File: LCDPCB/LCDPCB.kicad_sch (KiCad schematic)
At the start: 31 parts, among them J1 Sockets, J2 Hot Plug, J3 Programming Header, J4 Conn_01x08_Male, J5 Conn_01x08_Male, SW1 SW_Push, U1 STM32F091RCT6, U2 LD1117S12TR_SOT223

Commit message: minor
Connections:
- net +3.3V: now also C4.1, C5.1, D2.2 (A), U2.2 (VO)
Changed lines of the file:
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@@
   (junction (at 149.86 52.07) (diameter 0) (color 0 0 0 0)
+  )
+  (junction (at 63.5 74.93) (diameter 0) (color 0 0 0 0)
   )
   (junction (at 54.61 101.6) (diameter 0) (color 0 0 0 0)
@@
     (stroke (width 0) (type default) (color 0 0 0 0))
   )
+  (wire (pts (xy 63.5 74.93) (xy 69.85 74.93))
+    (stroke (width 0) (type default) (color 0 0 0 0))
+  )
   (polyline (pts (xy 81.28 55.88) (xy 21.59 55.88))
     (stroke (width 0) (type default) (color 0 0 0 0))
@@
     (stroke (width 0) (type default) (color 0 0 0 0))
   )
-  (wire (pts (xy 59.69 74.93) (xy 69.85 74.93))
+  (wire (pts (xy 59.69 74.93) (xy 63.5 74.93))
     (stroke (width 0) (type default) (color 0 0 0 0))
   )
@@
     (pin "1")
   )
+  (symbol (lib_id "power:+3.3V") (at 63.5 74.93 0) (unit 1)
+    (in_bom yes) (on_board yes) (fields_autoplaced)
+    (property "Reference" "#PWR?" (id 0) (at 63.5 78.74 0)
+      (effects (font (size 1.27 1.27)) hide)
+    )
+    (property "Value" "+3.3V" (id 1) (at 63.5 69.85 0))
+    (property "Footprint" "" (id 2) (at 63.5 74.93 0)
+      (effects (font (size 1.27 1.27)) hide)
+    )
+    (property "Datasheet" "" (id 3) (at 63.5 74.93 0)
+      (effects (font (size 1.27 1.27)) hide)
+    )
+    (pin "1")
+  )
   (symbol (lib_id "power:+3V0") (at 242.57 25.4 0) (unit 1)
     (in_bom yes) (on_board yes) (fields_autoplaced)
@@
       (reference "#PWR0126") (unit 1) (value "+3.3V") (footprint "")
     )
+    (path "/ba82aeb4-706f-462a-8336-75695364b5b1"
+      (reference "#PWR?") (unit 1) (value "+3.3V") (footprint "")
+    )
     (path "/288a3ec0-122f-4360-968a-e07818d05bc7"

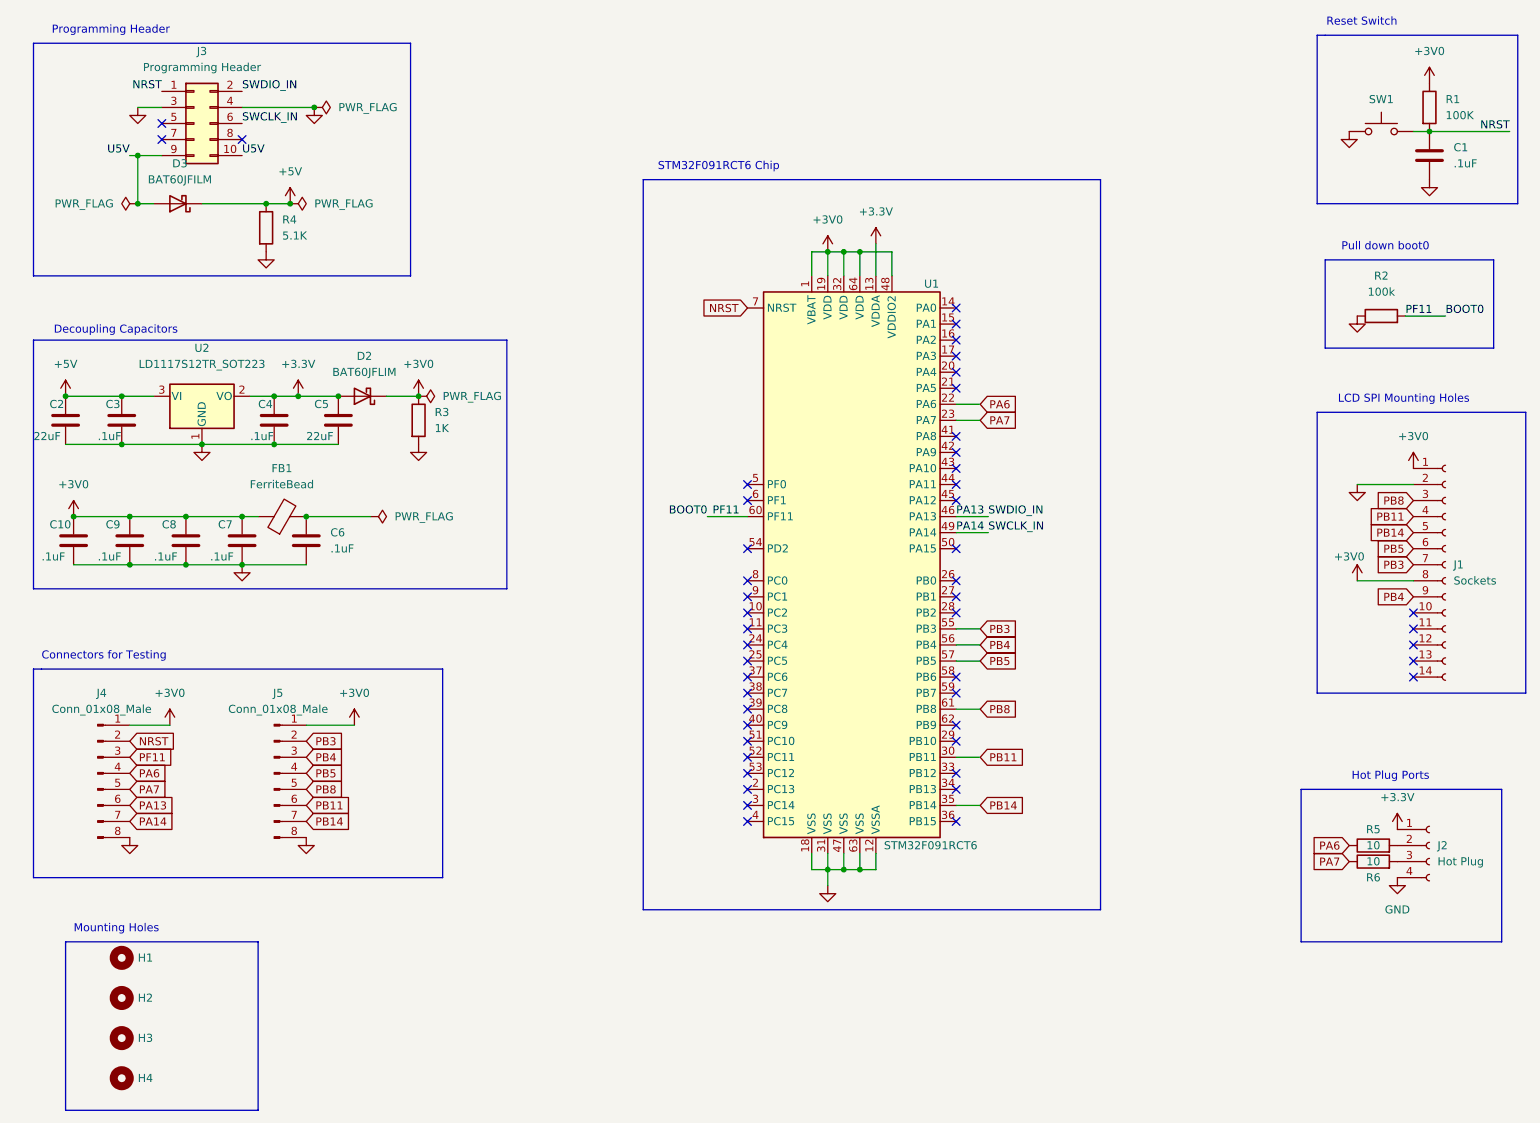
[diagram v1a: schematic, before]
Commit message: added thermal relief, made 5V routes wider
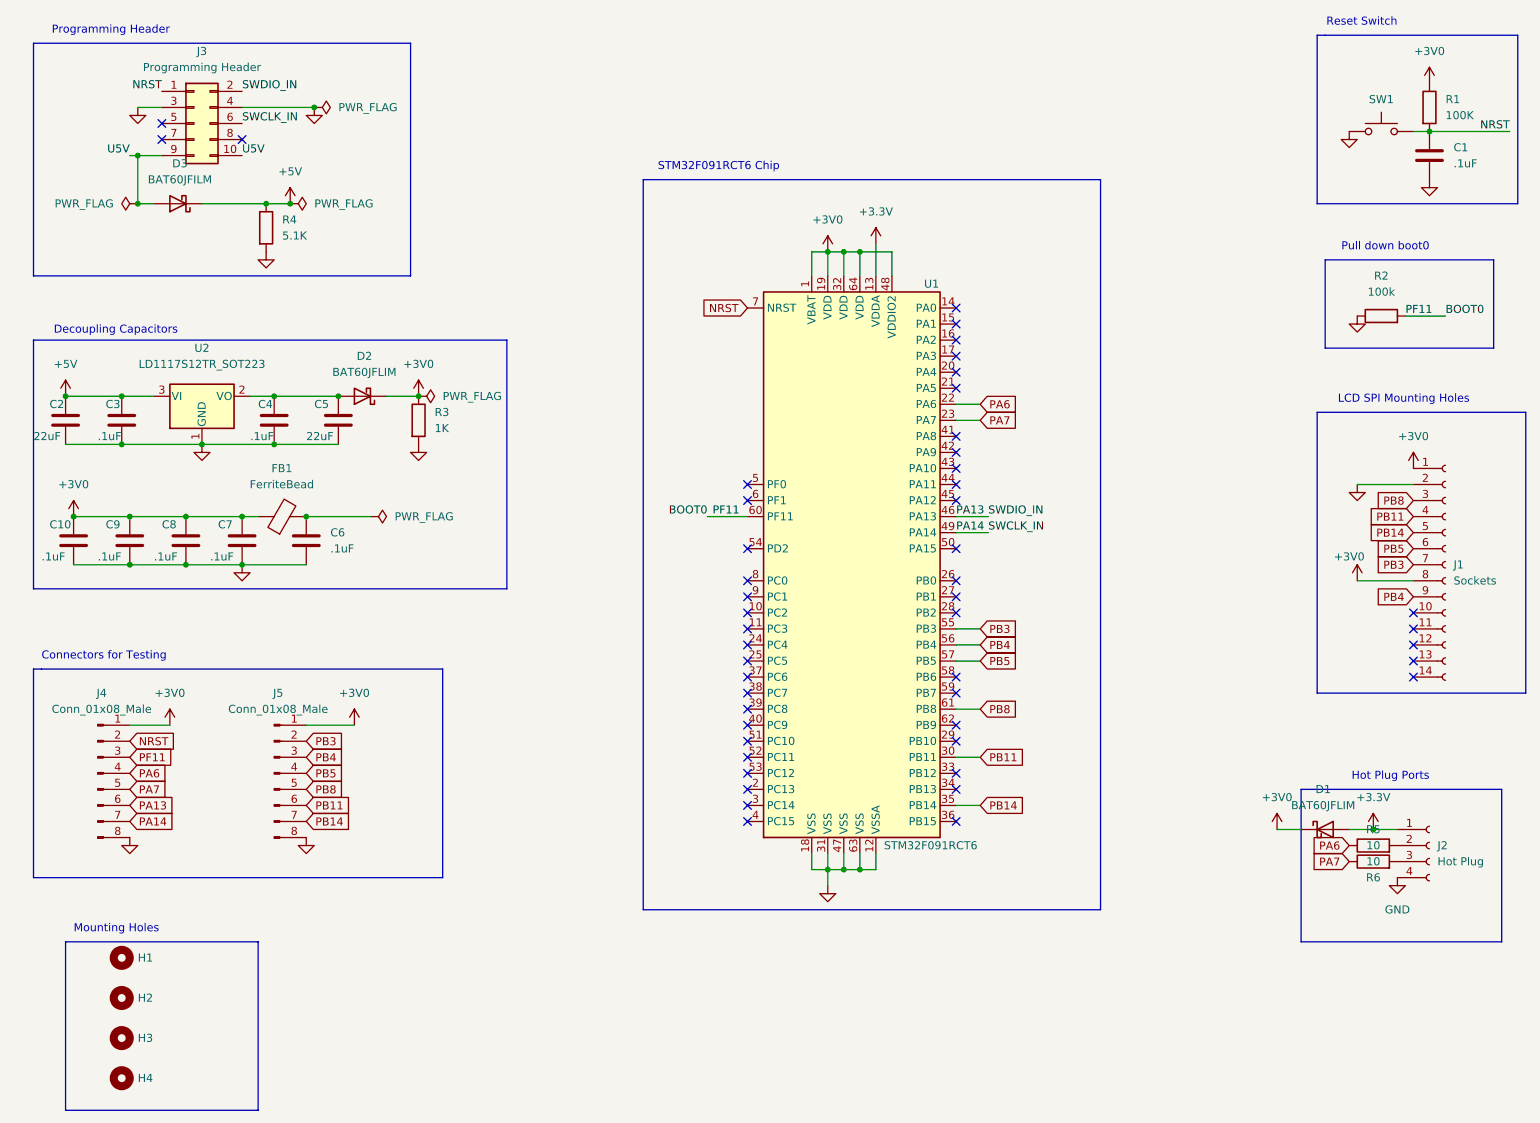
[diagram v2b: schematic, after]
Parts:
- added D1: BAT60JFLIM, lib_file:BAT60JFILM, symbol Diode:BAT60A
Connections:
- net +3.3V: now also D1.2 (A); no longer C4.1, C5.1, D2.2 (A), U2.2 (VO)
- net +3V0: now also D1.1 (K)
- new net: C4.1, C5.1, D2.2 (A), U2.2 (VO)
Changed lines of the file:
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@@
   (junction (at 36.83 101.6) (diameter 0) (color 0 0 0 0)
   )
+  (junction (at 233.68 143.51) (diameter 0) (color 0 0 0 0)
+  )
   (junction (at 62.23 44.45) (diameter 0) (color 0 0 0 0)
   )
@@
   )
   (junction (at 149.86 52.07) (diameter 0) (color 0 0 0 0)
-  )
-  (junction (at 63.5 74.93) (diameter 0) (color 0 0 0 0)
   )
   (junction (at 54.61 101.6) (diameter 0) (color 0 0 0 0)
@@
     (stroke (width 0) (type default) (color 0 0 0 0))
   )
+  (wire (pts (xy 229.87 143.51) (xy 233.68 143.51))
+    (stroke (width 0) (type default) (color 0 0 0 0))
+  )
   (polyline (pts (xy 21.59 118.11) (xy 22.86 118.11))
     (stroke (width 0) (type default) (color 0 0 0 0))
@@
     (stroke (width 0) (type default) (color 0 0 0 0))
   )
-  (wire (pts (xy 63.5 74.93) (xy 69.85 74.93))
+  (wire (pts (xy 59.69 74.93) (xy 69.85 74.93))
     (stroke (width 0) (type default) (color 0 0 0 0))
   )
@@
     (stroke (width 0) (type default) (color 0 0 0 0))
   )
+  (wire (pts (xy 218.44 143.51) (xy 222.25 143.51))
+    (stroke (width 0) (type default) (color 0 0 0 0))
+  )
   (wire (pts (xy 36.83 101.6) (xy 45.72 101.6))
     (stroke (width 0) (type default) (color 0 0 0 0))
@@
     (stroke (width 0) (type default) (color 0 0 0 0))
   )
+  (wire (pts (xy 233.68 143.51) (xy 237.49 143.51))
+    (stroke (width 0) (type default) (color 0 0 0 0))
+  )
   (wire (pts (xy 147.32 52.07) (xy 149.86 52.07))
     (stroke (width 0) (type default) (color 0 0 0 0))
@@
   )
   (wire (pts (xy 77.47 74.93) (xy 82.55 74.93))
-    (stroke (width 0) (type default) (color 0 0 0 0))
-  )
-  (wire (pts (xy 59.69 74.93) (xy 63.5 74.93))
     (stroke (width 0) (type default) (color 0 0 0 0))
   )
@@
     (pin "2")
   )
+  (symbol (lib_id "Diode:BAT60A") (at 226.06 143.51 0) (unit 1)
+    (in_bom yes) (on_board yes) (fields_autoplaced)
+    (property "Reference" "D1" (id 0) (at 225.7425 137.16 0))
+    (property "Value" "BAT60JFLIM" (id 1) (at 225.7425 139.7 0))
+    (property "Footprint" "lib_file:BAT60JFILM" (id 2) (at 226.06 147.955 0)
+      (effects (font (size 1.27 1.27)) hide)
+    )
+    (property "Datasheet" "https://www.infineon.com/dgdl/Infineon-BAT60ASERIES-DS-v01_01-en.pdf?fileId=db3a304313d846880113def70c9304a9" (id 3) (at 226.06 143.51 0)
+      (effects (font (size 1.27 1.27)) hide)
+    )
+    (pin "1")
+    (pin "2")
+  )
   (symbol (lib_id "power:GND") (at 231.14 88.9 0) (unit 1)
     (in_bom yes) (on_board yes) (fields_autoplaced)
@@
     (pin "1")
   )
-  (symbol (lib_id "power:+3.3V") (at 237.49 143.51 0) (unit 1)
-    (in_bom yes) (on_board yes) (fields_autoplaced)
-    (property "Reference" "#PWR0102" (id 0) (at 237.49 147.32 0)
-      (effects (font (size 1.27 1.27)) hide)
-    )
-    (property "Value" "+3.3V" (id 1) (at 237.49 138.43 0))
-    (property "Footprint" "" (id 2) (at 237.49 143.51 0)
-      (effects (font (size 1.27 1.27)) hide)
-    )
-    (property "Datasheet" "" (id 3) (at 237.49 143.51 0)
+  (symbol (lib_id "power:+3.3V") (at 233.68 143.51 0) (unit 1)
+    (in_bom yes) (on_board yes) (fields_autoplaced)
+    (property "Reference" "#PWR0102" (id 0) (at 233.68 147.32 0)
+      (effects (font (size 1.27 1.27)) hide)
+    )
+    (property "Value" "+3.3V" (id 1) (at 233.68 138.43 0))
+    (property "Footprint" "" (id 2) (at 233.68 143.51 0)
+      (effects (font (size 1.27 1.27)) hide)
+    )
+    (property "Datasheet" "" (id 3) (at 233.68 143.51 0)
       (effects (font (size 1.27 1.27)) hide)
     )
@@
     (pin "1")
   )
-  (symbol (lib_id "power:+3.3V") (at 63.5 74.93 0) (unit 1)
-    (in_bom yes) (on_board yes) (fields_autoplaced)
-    (property "Reference" "#PWR?" (id 0) (at 63.5 78.74 0)
-      (effects (font (size 1.27 1.27)) hide)
-    )
-    (property "Value" "+3.3V" (id 1) (at 63.5 69.85 0))
-    (property "Footprint" "" (id 2) (at 63.5 74.93 0)
-      (effects (font (size 1.27 1.27)) hide)
-    )
-    (property "Datasheet" "" (id 3) (at 63.5 74.93 0)
-      (effects (font (size 1.27 1.27)) hide)
-    )
-    (pin "1")
-  )
   (symbol (lib_id "power:+3V0") (at 242.57 25.4 0) (unit 1)
     (in_bom yes) (on_board yes) (fields_autoplaced)
@@
     (pin "1")
   )
+  (symbol (lib_id "power:+3V0") (at 218.44 143.51 0) (unit 1)
+    (in_bom yes) (on_board yes) (fields_autoplaced)
+    (property "Reference" "#PWR0127" (id 0) (at 218.44 147.32 0)
+      (effects (font (size 1.27 1.27)) hide)
+    )
+    (property "Value" "+3V0" (id 1) (at 218.44 138.43 0))
+    (property "Footprint" "" (id 2) (at 218.44 143.51 0)
+      (effects (font (size 1.27 1.27)) hide)
+    )
+    (property "Datasheet" "" (id 3) (at 218.44 143.51 0)
+      (effects (font (size 1.27 1.27)) hide)
+    )
+    (pin "1")
+  )
   (symbol (lib_id "power:+3V0") (at 43.18 127 0) (unit 1)
     (in_bom yes) (on_board yes) (fields_autoplaced)
@@
       (reference "#PWR0126") (unit 1) (value "+3.3V") (footprint "")
     )
-    (path "/ba82aeb4-706f-462a-8336-75695364b5b1"
-      (reference "#PWR?") (unit 1) (value "+3.3V") (footprint "")
+    (path "/d3d6295b-34fe-4b57-b4ca-7c0f40dd5880"
+      (reference "#PWR0127") (unit 1) (value "+3V0") (footprint "")
     )
     (path "/288a3ec0-122f-4360-968a-e07818d05bc7"
@@
       (reference "C10") (unit 1) (value ".1uF") (footprint "lib_file:.1uF")
     )
+    (path "/02267eaf-79b9-48e0-976b-998c9a2d1fd7"
+      (reference "D1") (unit 1) (value "BAT60JFLIM") (footprint "lib_file:BAT60JFILM")
+    )
     (path "/f3eeaca9-01b9-45ab-a60b-99a2befb5b1d"

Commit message: added thermal reliefs
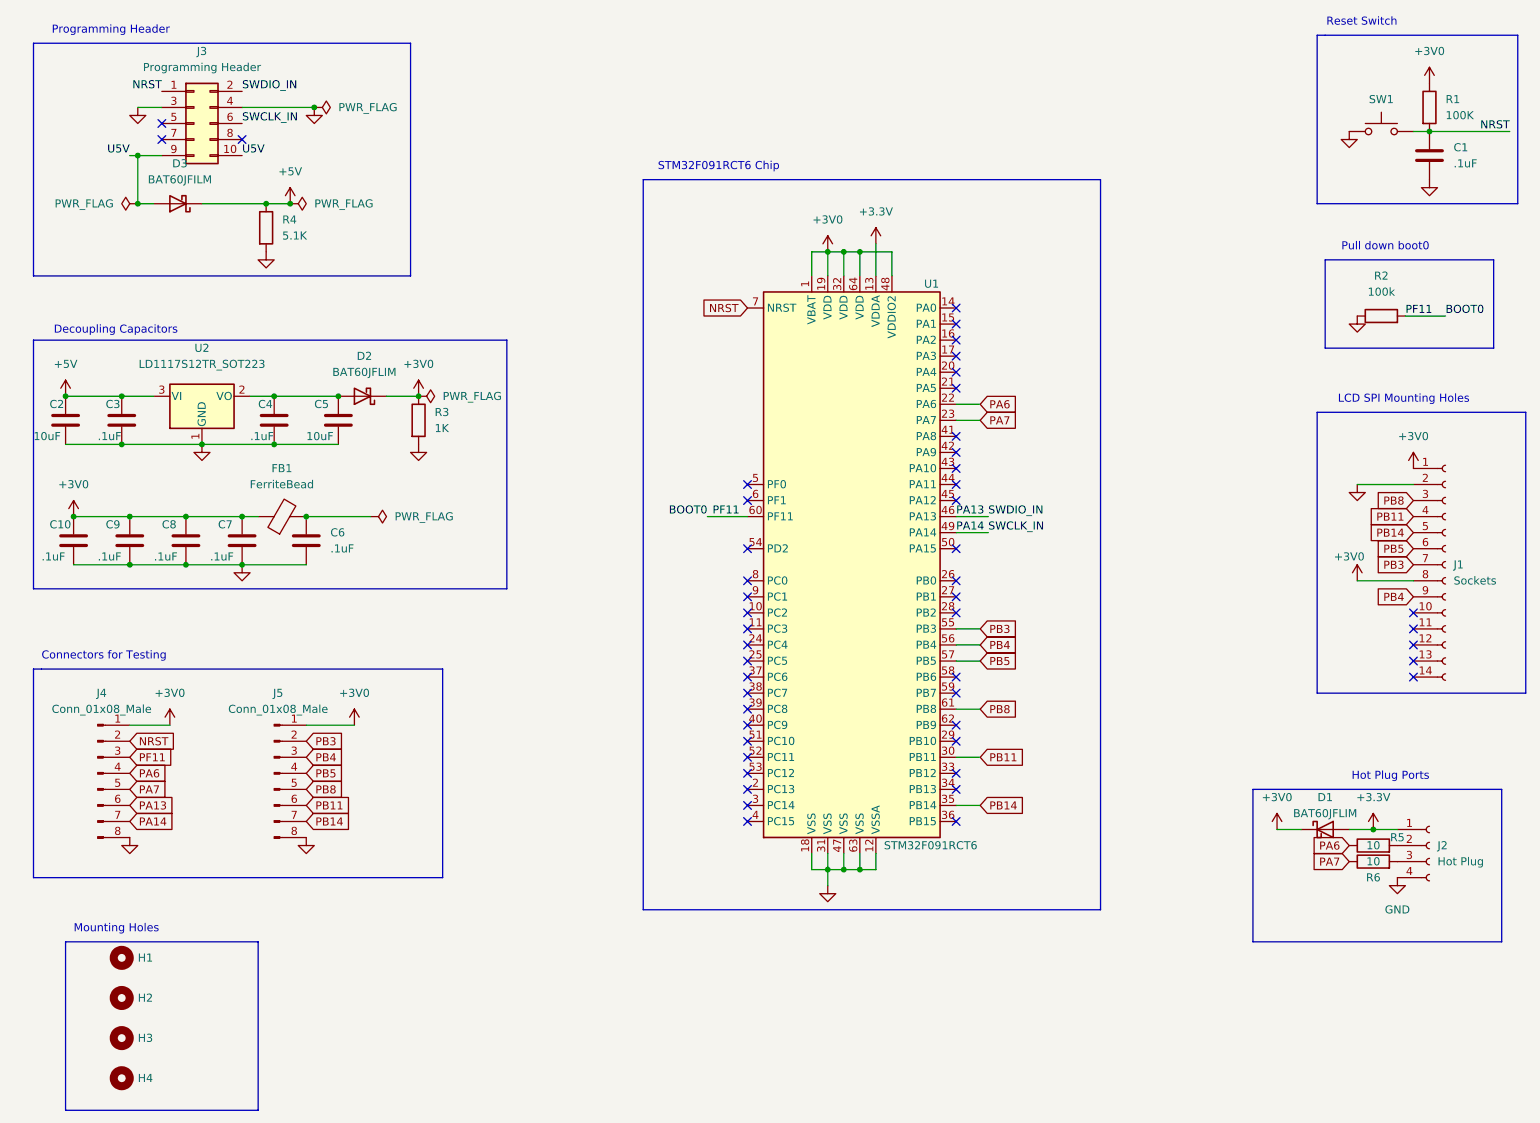
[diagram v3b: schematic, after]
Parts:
- C2: value 22uF -> 10uF; footprint lib_file:22uFC -> lib_file:10uF
- C5: value 22uF -> 10uF; footprint lib_file:22uF -> lib_file:10uF
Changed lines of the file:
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@@
     (stroke (width 0) (type default) (color 0 0 0 0))
   )
-  (polyline (pts (xy 222.25 137.16) (xy 222.25 161.29))
+  (polyline (pts (xy 214.63 137.16) (xy 214.63 161.29))
     (stroke (width 0) (type default) (color 0 0 0 0))
   )
@@
     (stroke (width 0) (type default) (color 0 0 0 0))
   )
-  (polyline (pts (xy 254 161.29) (xy 222.25 161.29))
+  (polyline (pts (xy 254 161.29) (xy 214.63 161.29))
     (stroke (width 0) (type default) (color 0 0 0 0))
   )
@@
     (stroke (width 0) (type default) (color 0 0 0 0))
   )
-  (polyline (pts (xy 222.25 137.16) (xy 254 137.16))
+  (polyline (pts (xy 214.63 137.16) (xy 254 137.16))
     (stroke (width 0) (type default) (color 0 0 0 0))
   )
@@
   )
   (symbol (lib_id "Diode:BAT60A") (at 226.06 143.51 0) (unit 1)
-    (in_bom yes) (on_board yes) (fields_autoplaced)
-    (property "Reference" "D1" (id 0) (at 225.7425 137.16 0))
-    (property "Value" "BAT60JFLIM" (id 1) (at 225.7425 139.7 0))
+    (in_bom yes) (on_board yes)
+    (property "Reference" "D1" (id 0) (at 226.06 138.43 0))
+    (property "Value" "BAT60JFLIM" (id 1) (at 226.06 140.97 0))
     (property "Footprint" "lib_file:BAT60JFILM" (id 2) (at 226.06 147.955 0)
       (effects (font (size 1.27 1.27)) hide)
@@
       (effects (font (size 1.27 1.27)) (justify left))
     )
-    (property "Value" "22uF" (id 1) (at 64.77 81.28 0)
-      (effects (font (size 1.27 1.27)) (justify left))
-    )
-    (property "Footprint" "lib_file:22uF" (id 2) (at 70.8152 82.55 0)
+    (property "Value" "10uF" (id 1) (at 64.77 81.28 0)
+      (effects (font (size 1.27 1.27)) (justify left))
+    )
+    (property "Footprint" "lib_file:10uF" (id 2) (at 70.8152 82.55 0)
       (effects (font (size 1.27 1.27)) hide)
     )
@@
   (symbol (lib_id "Device:R") (at 233.68 146.05 90) (unit 1)
     (in_bom yes) (on_board yes)
-    (property "Reference" "R5" (id 0) (at 233.68 143.51 90))
+    (property "Reference" "R5" (id 0) (at 237.49 144.78 90))
     (property "Value" "10" (id 1) (at 233.68 146.05 90))
     (property "Footprint" "lib_file:10R" (id 2) (at 233.68 147.828 90)
@@
       (effects (font (size 1.27 1.27)) (justify left))
     )
-    (property "Value" "22uF" (id 1) (at 21.59 81.28 0)
-      (effects (font (size 1.27 1.27)) (justify left))
-    )
-    (property "Footprint" "lib_file:22uFC" (id 2) (at 27.6352 82.55 0)
+    (property "Value" "10uF" (id 1) (at 21.59 81.28 0)
+      (effects (font (size 1.27 1.27)) (justify left))
+    )
+    (property "Footprint" "lib_file:10uF" (id 2) (at 27.6352 82.55 0)
       (effects (font (size 1.27 1.27)) hide)
     )
@@
     )
     (path "/f24fd606-4838-4530-b0e3-89032e781ead"
-      (reference "C2") (unit 1) (value "22uF") (footprint "lib_file:22uFC")
+      (reference "C2") (unit 1) (value "10uF") (footprint "lib_file:10uF")
     )
     (path "/5da5ad4e-2433-4ba1-8c71-f4c200e15d6f"
@@
     )
     (path "/539f87f9-cf10-45cd-a5d1-7d1a9d2a2b8f"
-      (reference "C5") (unit 1) (value "22uF") (footprint "lib_file:22uF")
+      (reference "C5") (unit 1) (value "10uF") (footprint "lib_file:10uF")
     )
     (path "/5a769286-a8c8-4ba6-bd0a-7d58c48ddf5f"

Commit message: do you love me now dad?
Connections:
- net SCL: now reaches U1.58 (PB6)
- net SCL: now also J4.4 (Pin_4), R5.1
- net SDA: now reaches U1.59 (PB7)
- net SDA: now also J4.5 (Pin_5), R6.1
- removed net PA6: J4.4 (Pin_4), R5.1, U1.22 (PA6)
- removed net PA7: J4.5 (Pin_5), R6.1, U1.23 (PA7)
- net PB11 renamed RESET
- net PB14 renamed DC
- net PB3 renamed SCK
- net PB4 renamed MISO
- net PB5 renamed MOSI
- net PB8 renamed CS
- net PF11 renamed PD

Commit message: edits
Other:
- moved on the sheet: D1, J2, R5, R6

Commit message: submodule casing files
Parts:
- C2: footprint lib_file:10uF -> lib_file:new10uf
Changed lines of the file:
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@@
       (effects (font (size 1.27 1.27)) (justify left))
     )
-    (property "Footprint" "lib_file:10uF" (id 2) (at 27.6352 82.55 0)
+    (property "Footprint" "lib_file:new10uf" (id 2) (at 27.6352 82.55 0)
       (effects (font (size 1.27 1.27)) hide)
     )
@@
     )
     (path "/f24fd606-4838-4530-b0e3-89032e781ead"
-      (reference "C2") (unit 1) (value "10uF") (footprint "lib_file:10uF")
+      (reference "C2") (unit 1) (value "10uF") (footprint "lib_file:new10uf")
     )
     (path "/5da5ad4e-2433-4ba1-8c71-f4c200e15d6f"
